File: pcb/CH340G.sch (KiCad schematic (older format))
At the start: 5 parts

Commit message: changed LED and boost converters Diode footprints. renumbered components
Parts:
- gave numbers to parts that had none: 5
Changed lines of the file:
@@
 $EndDescr
 $Comp
-L CH340G IC?
+L CH340G IC401
 U 1 1 58D8F874
 P 6350 3550
-F 0 "IC?" H 6150 4150 60  0000 C CNN
+F 0 "IC401" H 6150 4150 60  0000 C CNN
 F 1 "CH340G" H 6350 4050 60  0000 C CNN
 F 2 "Housings_SOIC:SOIC-16_3.9x9.9mm_Pitch1.27mm" H 6350 3550 60  0001 C CNN
@@
 $EndComp
 $Comp
-L GND #PWR?
+L GND #PWR403
 U 1 1 58D8F87B
 P 5850 4200
-F 0 "#PWR?" H 5850 3950 50  0001 C CNN
+F 0 "#PWR403" H 5850 3950 50  0001 C CNN
 F 1 "GND" H 5850 4050 50  0000 C CNN
 F 2 "" H 5850 4200 50  0000 C CNN
@@
 $EndComp
 $Comp
-L GND #PWR?
+L GND #PWR402
 U 1 1 58D8F885
 P 5250 4200
-F 0 "#PWR?" H 5250 3950 50  0001 C CNN
+F 0 "#PWR402" H 5250 3950 50  0001 C CNN
 F 1 "GND" H 5250 4050 50  0000 C CNN
 F 2 "" H 5250 4200 50  0000 C CNN
@@
 $EndComp
 $Comp
-L C C?
+L C C402
 U 1 1 58D8F88B
 P 4850 3950
-F 0 "C?" H 4875 4050 50  0000 L CNN
+F 0 "C402" H 4875 4050 50  0000 L CNN
 F 1 "22p" H 4875 3850 50  0000 L CNN
 F 2 "netl:SMD_0603" H 4888 3800 50  0001 C CNN
@@
 $EndComp
 $Comp
-L C C?
+L C C403
 U 1 1 58D8F892
 P 5650 3950
-F 0 "C?" H 5675 4050 50  0000 L CNN
+F 0 "C403" H 5675 4050 50  0000 L CNN
 F 1 "22p" H 5675 3850 50  0000 L CNN
 F 2 "netl:SMD_0603" H 5688 3800 50  0001 C CNN
@@
 Connection ~ 5650 3750
 $Comp
-L xtal_osc x?
+L xtal_osc x401
 U 1 1 58D8F8A6
 P 5250 3750
-F 0 "x?" H 5100 4000 60  0000 C CNN
+F 0 "x401" H 5100 4000 60  0000 C CNN
 F 1 "xtal_osc" H 5250 3900 60  0000 C CNN
 F 2 "netl:SM_3225" H 5250 3800 60  0001 C CNN
@@
 	6950 3450 6800 3450
 $Comp
-L C C?
+L C C401
 U 1 1 58D8F8C0
 P 4550 3650
-F 0 "C?" H 4575 3750 50  0000 L CNN
+F 0 "C401" H 4575 3750 50  0000 L CNN
 F 1 "10u" H 4575 3550 50  0000 L CNN
 F 2 "netl:SMD_0603" H 4588 3500 50  0001 C CNN
@@
 $EndComp
 $Comp
-L GND #PWR?
+L GND #PWR401
 U 1 1 58D8F8C7
 P 4550 4200
-F 0 "#PWR?" H 4550 3950 50  0001 C CNN
+F 0 "#PWR401" H 4550 3950 50  0001 C CNN
 F 1 "GND" H 4550 4050 50  0000 C CNN
 F 2 "" H 4550 4200 50  0000 C CNN

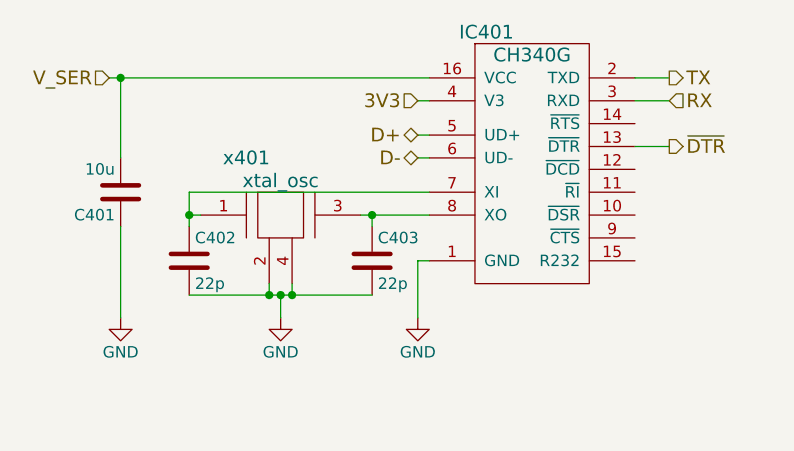
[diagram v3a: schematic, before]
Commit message: finished swapping parts, started layout
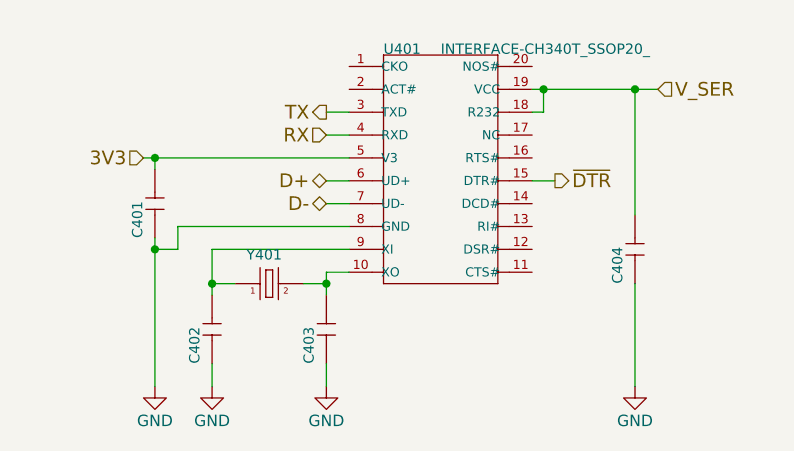
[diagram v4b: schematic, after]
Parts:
- removed C401: 10u, netl:SMD_0603, symbol C
- removed C402, C403: 22p, netl:SMD_0603, symbol C
- removed IC401: CH340G, Housings_SOIC:SOIC-16_3.9x9.9mm_Pitch1.27mm, symbol CH340G
- removed x401: xtal_osc, netl:SM_3225, symbol xtal_osc
- added C401, C404: CERAMIC-100NF-50V-10%-X7R_0603_, SeeedOPL-Capacitor-2016:C0603, symbol CERAMIC-100NF-50V-10%-X7R_0603_
- added C402, C403: CERAMIC-22PF-50V-5%-NPO_0603_, SeeedOPL-Capacitor-2016:C0603, symbol CERAMIC-22PF-50V-5%-NPO_0603_
- added U401: INTERFACE-CH340T_SSOP20_, SeeedOPL-IC-2016:TSSOP20-0.65-6.5X4.4MM, symbol INTERFACE-CH340T_SSOP20_
- added Y401: SMD-CRYSTAL-12MHZ-20PF-20PPM-40R_2P-5.0X3.2MM_, SeeedOPL-Crystal Oscillator-2016:X2-SMD-5.0X3.2X1.3MM, symbol SMD-CRYSTAL-12MHZ-20PF-20PPM-40R_2P-5.0X3.2MM_
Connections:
- net 3V3: now also C401.2, U401.5 (V3)
- net D+: now also U401.6 (UD+)
- net D-: now also U401.7 (UD-)
- net GND: now also C401.1, C402.1, C403.1, C404.1, U401.8 (GND)
- net RX: now also U401.4 (RXD)
- net TX: now also U401.3 (TXD)
- net V_SER: now also C404.2, U401.18 (R232), U401.19 (VCC)
- net ~DTR: now also U401.15 (DTR#)
- new net: C403.2, U401.10 (XO), Y401.2
- new net: C402.2, U401.9 (XI), Y401.1
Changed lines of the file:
@@
 $EndDescr
 $Comp
-L CH340G IC401
-U 1 1 58D8F874
-P 6350 3550
-F 0 "IC401" H 6150 4150 60  0000 C CNN
-F 1 "CH340G" H 6350 4050 60  0000 C CNN
-F 2 "Housings_SOIC:SOIC-16_3.9x9.9mm_Pitch1.27mm" H 6350 3550 60  0001 C CNN
-F 3 "" H 6350 3550 60  0000 C CNN
-	1    6350 3550
+L INTERFACE-CH340T_SSOP20_ U401
+U 1 1 5A553226
+P 5950 3550
+F 0 "U401" H 5700 4050 45  0000 L BNN
+F 1 "INTERFACE-CH340T_SSOP20_" H 5950 4050 45  0000 L BNN
+F 2 "SeeedOPL-IC-2016:TSSOP20-0.65-6.5X4.4MM" H 5950 3550 60  0001 C CNN
+F 3 "" H 5950 3550 60  0001 C CNN
+F 4 "CH340T" H 5980 3700 20  0001 C CNN "MPN"
+F 5 "310070026" H 5980 3700 20  0001 C CNN "SKU"
+	1    5950 3550
+	1    0    0    -1
+$EndComp
+Text HLabel 6450 3600 2    60   Output ~ 0
+~DTR
+Text HLabel 5450 3400 0    60   Input ~ 0
+RX
+Text HLabel 5450 3300 0    60   Output ~ 0
+TX
+Text HLabel 6900 3200 2    60   Input ~ 0
+V_SER
+Text HLabel 4650 3500 0    60   Input ~ 0
+3V3
+Wire Wire Line
+	6450 3600 6350 3600
+Wire Wire Line
+	6350 3200 6900 3200
+Wire Wire Line
+	6350 3300 6400 3300
+Wire Wire Line
+	6400 3300 6400 3200
+Connection ~ 6400 3200
+Wire Wire Line
+	5550 3400 5450 3400
+Wire Wire Line
+	5550 3300 5450 3300
+Wire Wire Line
+	4650 3500 5550 3500
+$Comp
+L CERAMIC-100NF-50V-10%-X7R_0603_ C404
+U 1 1 5A553863
+P 6800 3900
+F 0 "C404" H 6650 3950 45  0000 L BNN
+F 1 "CERAMIC-100NF-50V-10%-X7R_0603_" H 6650 3800 45  0001 L BNN
+F 2 "SeeedOPL-Capacitor-2016:C0603" H 6800 3900 60  0001 C CNN
+F 3 "" H 6800 3900 60  0001 C CNN
+F 4 "CC0603KRX7R9BB104" H 6830 4050 20  0001 C CNN "MPN"
+F 5 "302010138" H 6830 4050 20  0001 C CNN "SKU"
+	1    6800 3900
+	0    -1   -1   0
+$EndComp
+$Comp
+L CERAMIC-100NF-50V-10%-X7R_0603_ C401
+U 1 1 5A553922
+P 4700 3700
+F 0 "C401" H 4550 3750 45  0000 L BNN
+F 1 "CERAMIC-100NF-50V-10%-X7R_0603_" H 4550 3600 45  0001 L BNN
+F 2 "SeeedOPL-Capacitor-2016:C0603" H 4700 3700 60  0001 C CNN
+F 3 "" H 4700 3700 60  0001 C CNN
+F 4 "CC0603KRX7R9BB104" H 4730 3850 20  0001 C CNN "MPN"
+F 5 "302010138" H 4730 3850 20  0001 C CNN "SKU"
+	1    4700 3700
+	0    -1   -1   0
+$EndComp
+Wire Wire Line
+	5550 3800 4800 3800
+Wire Wire Line
+	4700 3550 4700 3500
+Connection ~ 4700 3500
+Wire Wire Line
+	4700 3850 4700 4500
+$Comp
+L GND #PWR025
+U 1 1 5A553B10
+P 4700 4500
+F 0 "#PWR025" H 4700 4250 50  0001 C CNN
+F 1 "GND" H 4700 4350 50  0000 C CNN
+F 2 "" H 4700 4500 50  0001 C CNN
+F 3 "" H 4700 4500 50  0001 C CNN
+	1    4700 4500
+	1    0    0    -1
+$EndComp
+Wire Wire Line
+	4800 3800 4800 3900
+Wire Wire Line
+	4800 3900 4700 3900
+Connection ~ 4700 3900
+$Comp
+L GND #PWR026
+U 1 1 5A553C9B
+P 6800 4500
+F 0 "#PWR026" H 6800 4250 50  0001 C CNN
+F 1 "GND" H 6800 4350 50  0000 C CNN
+F 2 "" H 6800 4500 50  0001 C CNN
+F 3 "" H 6800 4500 50  0001 C CNN
+	1    6800 4500
+	1    0    0    -1
+$EndComp
+Wire Wire Line
+	6800 4050 6800 4500
+Wire Wire Line
+	6800 3750 6800 3200
+Connection ~ 6800 3200
+Text HLabel 5450 3600 0    60   BiDi ~ 0
+D+
+Text HLabel 5450 3700 0    60   BiDi ~ 0
+D-
+$Comp
+L SMD-CRYSTAL-12MHZ-20PF-20PPM-40R_2P-5.0X3.2MM_ Y401
+U 1 1 5A553F82
+P 5200 4050
+F 0 "Y401" H 5100 4150 45  0000 L BNN
+F 1 "SMD-CRYSTAL-12MHZ-20PF-20PPM-40R_2P-5.0X3.2MM_" H 5100 3900 45  0001 L BNN
+F 2 "SeeedOPL-Crystal Oscillator-2016:X2-SMD-5.0X3.2X1.3MM" H 5200 4050 60  0001 C CNN
+F 3 "" H 5200 4050 60  0001 C CNN
+F 4 "5032_2P" H 5230 4200 20  0001 C CNN "MPN"
+F 5 "306010047" H 5230 4200 20  0001 C CNN "SKU"
+	1    5200 4050
 	1    0    0    -1
 $EndComp
 $Comp
 L GND #PWR027
-U 1 1 58D8F87B
-P 5850 4200
-F 0 "#PWR027" H 5850 3950 50  0001 C CNN
-F 1 "GND" H 5850 4050 50  0000 C CNN
-F 2 "" H 5850 4200 50  0000 C CNN
-F 3 "" H 5850 4200 50  0000 C CNN
-	1    5850 4200
+U 1 1 5A5541E3
+P 4950 4500
+F 0 "#PWR027" H 4950 4250 50  0001 C CNN
+F 1 "GND" H 4950 4350 50  0000 C CNN
+F 2 "" H 4950 4500 50  0001 C CNN
+F 3 "" H 4950 4500 50  0001 C CNN
+	1    4950 4500
 	1    0    0    -1
 $EndComp
 $Comp
 L GND #PWR028
-U 1 1 58D8F885
-P 5250 4200
-F 0 "#PWR028" H 5250 3950 50  0001 C CNN
-F 1 "GND" H 5250 4050 50  0000 C CNN
-F 2 "" H 5250 4200 50  0000 C CNN
-F 3 "" H 5250 4200 50  0000 C CNN
-	1    5250 4200
+U 1 1 5A554209
+P 5450 4500
+F 0 "#PWR028" H 5450 4250 50  0001 C CNN
+F 1 "GND" H 5450 4350 50  0000 C CNN
+F 2 "" H 5450 4500 50  0001 C CNN
+F 3 "" H 5450 4500 50  0001 C CNN
+	1    5450 4500
 	1    0    0    -1
 $EndComp
 $Comp
-L C C402
-U 1 1 58D8F88B
-P 4850 3950
-F 0 "C402" H 4875 4050 50  0000 L CNN
-F 1 "22p" H 4875 3850 50  0000 L CNN
-F 2 "netl:SMD_0603" H 4888 3800 50  0001 C CNN
-F 3 "" H 4850 3950 50  0000 C CNN
-	1    4850 3950
-	1    0    0    -1
+L CERAMIC-22PF-50V-5%-NPO_0603_ C402
+U 1 1 5A554259
+P 4950 4250
+F 0 "C402" H 4800 4300 45  0000 L BNN
+F 1 "CERAMIC-22PF-50V-5%-NPO_0603_" H 4800 4150 45  0001 L BNN
+F 2 "SeeedOPL-Capacitor-2016:C0603" H 4950 4250 60  0001 C CNN
+F 3 "" H 4950 4250 60  0001 C CNN
+F 4 "CC0603JRNPO9BN220" H 4980 4400 20  0001 C CNN "MPN"
+F 5 "302010143" H 4980 4400 20  0001 C CNN "SKU"
+	1    4950 4250
+	0    -1   -1   0
 $EndComp
 $Comp
-L C C403
-U 1 1 58D8F892
-P 5650 3950
-F 0 "C403" H 5675 4050 50  0000 L CNN
-F 1 "22p" H 5675 3850 50  0000 L CNN
-F 2 "netl:SMD_0603" H 5688 3800 50  0001 C CNN
-F 3 "" H 5650 3950 50  0000 C CNN
-	1    5650 3950
-	1    0    0    -1
+L CERAMIC-22PF-50V-5%-NPO_0603_ C403
+U 1 1 5A554384
+P 5450 4250
+F 0 "C403" H 5300 4300 45  0000 L BNN
+F 1 "CERAMIC-22PF-50V-5%-NPO_0603_" H 5300 4150 45  0001 L BNN
+F 2 "SeeedOPL-Capacitor-2016:C0603" H 5450 4250 60  0001 C CNN
+F 3 "" H 5450 4250 60  0001 C CNN
+F 4 "CC0603JRNPO9BN220" H 5480 4400 20  0001 C CNN "MPN"
+F 5 "302010143" H 5480 4400 20  0001 C CNN "SKU"
+	1    5450 4250
+	0    -1   -1   0
 $EndComp
 Wire Wire Line
-	6950 3250 6800 3250
+	5450 4000 5450 4100
 Wire Wire Line
-	5900 3950 5850 3950
+	5450 4050 5350 4050
 Wire Wire Line
-	5850 3950 5850 4200
+	5050 4050 4950 4050
 Wire Wire Line
-	4500 3150 5900 3150
+	4950 3900 4950 4100
 Wire Wire Line
-	5850 3250 5900 3250
+	4950 4400 4950 4500
 Wire Wire Line
-	5850 3400 5900 3400
+	5450 4400 5450 4500
 Wire Wire Line
-	5900 3500 5850 3500
+	5550 4000 5450 4000
+Connection ~ 5450 4050
 Wire Wire Line
-	5600 3750 5900 3750
+	5550 3900 4950 3900
+Connection ~ 4950 4050
 Wire Wire Line
-	5650 3750 5650 3800
-Connection ~ 5650 3750
-$Comp
-L xtal_osc x401
-U 1 1 58D8F8A6
-P 5250 3750
-F 0 "x401" H 5100 4000 60  0000 C CNN
-F 1 "xtal_osc" H 5250 3900 60  0000 C CNN
-F 2 "netl:SM_3225" H 5250 3800 60  0001 C CNN
-F 3 "" H 5250 3800 60  0000 C CNN
-	1    5250 3750
-	1    0    0    -1
-$EndComp
+	5450 3600 5550 3600
 Wire Wire Line
-	4900 3750 4850 3750
-Wire Wire Line
-	4850 3650 4850 3800
-Wire Wire Line
-	5250 4100 5250 4200
-Wire Wire Line
-	4850 4100 5650 4100
-Connection ~ 5250 4100
-Wire Wire Line
-	5200 4050 5200 4100
-Connection ~ 5200 4100
-Wire Wire Line
-	5300 4050 5300 4100
-Connection ~ 5300 4100
-Wire Wire Line
-	4850 3650 5900 3650
-Connection ~ 4850 3750
-Wire Wire Line
-	6950 3450 6800 3450
-$Comp
-L C C401
-U 1 1 58D8F8C0
-P 4550 3650
-F 0 "C401" H 4575 3750 50  0000 L CNN
-F 1 "10u" H 4575 3550 50  0000 L CNN
-F 2 "netl:SMD_0603" H 4588 3500 50  0001 C CNN
-F 3 "" H 4550 3650 50  0000 C CNN
-	1    4550 3650
-	-1   0    0    1
-$EndComp
-$Comp
-L GND #PWR029
-U 1 1 58D8F8C7
-P 4550 4200
-F 0 "#PWR029" H 4550 3950 50  0001 C CNN
-F 1 "GND" H 4550 4050 50  0000 C CNN
-F 2 "" H 4550 4200 50  0000 C CNN
-F 3 "" H 4550 4200 50  0000 C CNN
-	1    4550 4200
-	1    0    0    -1
-$EndComp
-Wire Wire Line
-	4550 3800 4550 4200
-Wire Wire Line
-	4550 3500 4550 3150
-Connection ~ 4550 3150
-Text HLabel 4500 3150 0    60   Input ~ 0
-V_SER
-Text HLabel 5850 3250 0    60   Input ~ 0
-3V3
-Text HLabel 5850 3400 0    60   BiDi ~ 0
-D+
-Text HLabel 5850 3500 0    60   BiDi ~ 0
-D-
-Text HLabel 6950 3150 2    60   Output ~ 0
-TX
-Wire Wire Line
-	6800 3150 6950 3150
-Text HLabel 6950 3250 2    60   Input ~ 0
-RX
-Text HLabel 6950 3450 2    60   Output ~ 0
-~DTR
+	5550 3700 5450 3700
 $EndSCHEMATC
